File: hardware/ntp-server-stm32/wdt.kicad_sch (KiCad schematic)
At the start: 4 parts, among them U64 TPS3430WDRC

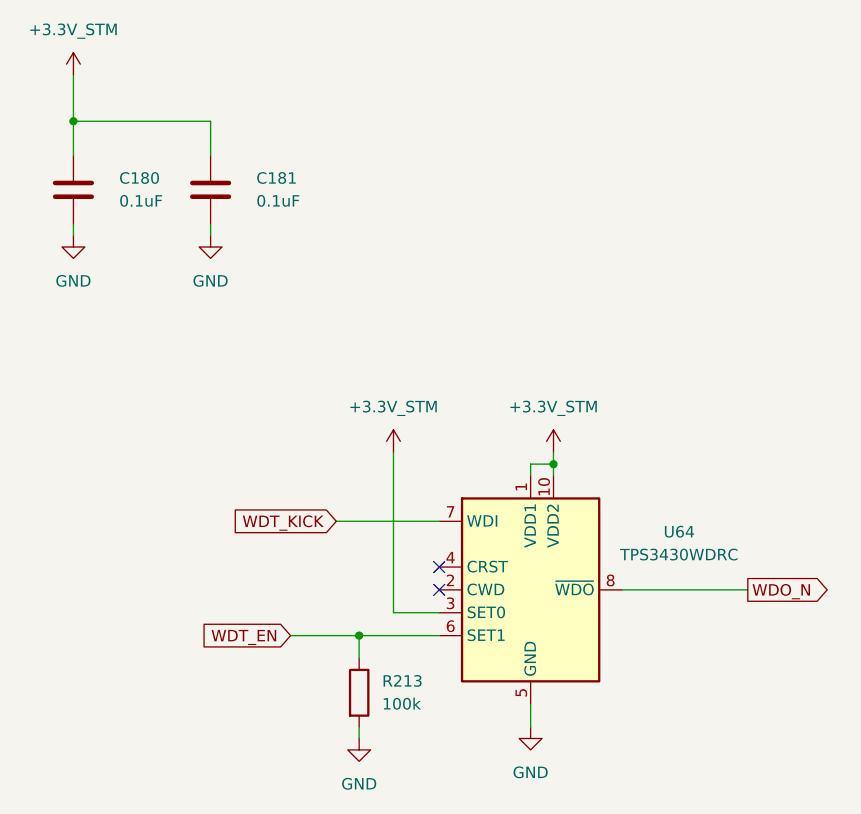
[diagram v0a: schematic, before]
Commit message: Standardize net/rail names: plain 3V3 style, _N active-low, voltage-format PG/alerts
22 net renames applied across all sheets and verified: removed/added net-name
sets match intent exactly and all node connectivity is preserved (kicad-cli
netlist re-parse).

Co-Authored-By: Claude Opus 4.8 (1M context) <noreply@anthropic.com>
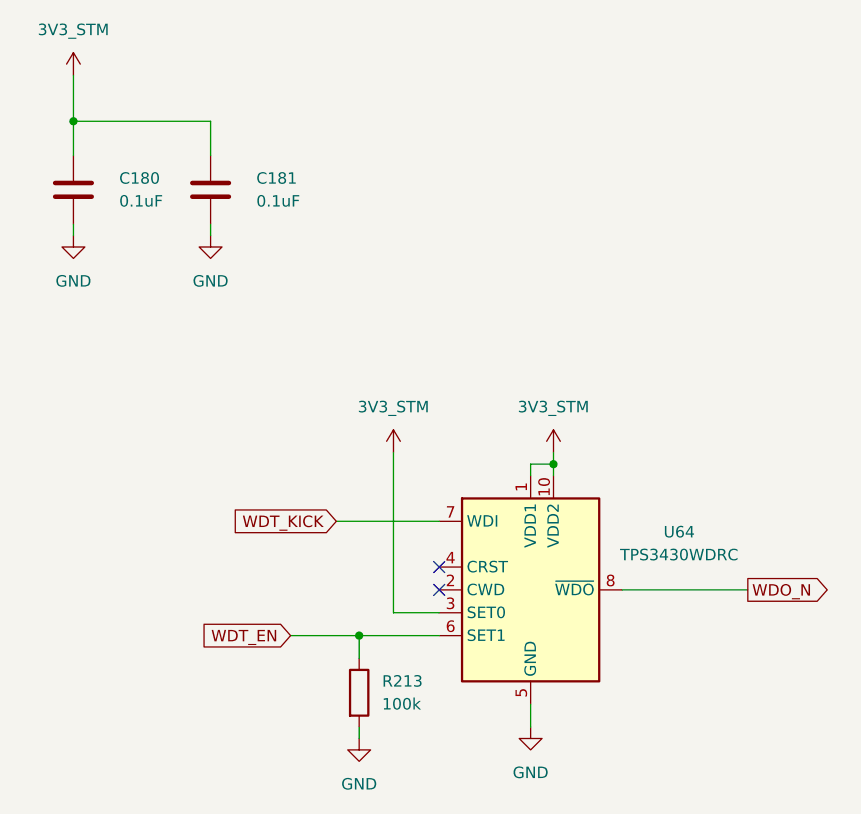
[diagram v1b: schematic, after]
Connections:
- net +3.3V_STM renamed 3V3_STM
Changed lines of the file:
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@@
 			)
 		)
-		(property "Value" "+3.3V_STM"
+		(property "Value" "3V3_STM"
 			(at 148.59 86.36 0)
 			(show_name no)
@@
 			)
 		)
-		(property "Value" "+3.3V_STM"
+		(property "Value" "3V3_STM"
 			(at 166.37 86.36 0)
 			(show_name no)
@@
 			)
 		)
-		(property "Value" "+3.3V_STM"
+		(property "Value" "3V3_STM"
 			(at 113.03 44.45 0)
 			(show_name no)

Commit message: Standardize + complete BOM; write fields back into KiCad symbols
- New sts1000_bom.csv: rebuilt from authoritative Value field (source MPN/footprint/
  description were corrupted by copy-paste). 338 standardized, 78 MPN-from-value,
  50 kept, ~64 flagged (SELECT/REVIEW-HV/SHUNT-REVIEW) each with full spec.
- Resistors -> deterministic Panasonic ERJ-2RKF 0402 1% 1/10W (consolidated 1 part/value).
- Caps -> verified Murata GRM parts where value matches; clean spec + footprint otherwise.
- 1633 symbol field updates (Value/Footprint/Description/MPN/Mfr/Digikey) written to
  .kicad_sch; netlist re-parse confirms connectivity byte-identical.
- Add docs/sts1000_net_naming.md naming reference.

Co-Authored-By: Claude Opus 4.8 (1M context) <noreply@anthropic.com>
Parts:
- C180, C181: footprint 0805 -> C_0402_1005Metric; DIGIKEY_PART_NUMBER 445-5972-1-ND -> 490-6328-2-ND; MANUFACTURER TDK -> Murata; MANUFACTURER_PART_NUMBER C2012X7R1E475K125AB -> GRM155R71C104KA88J
- R213: footprint (none) -> R_0402_1005Metric; MANUFACTURER (none) -> Panasonic; MANUFACTURER_PART_NUMBER (none) -> ERJ-2RKF1003X
- U64: MANUFACTURER_PART_NUMBER (none) -> TPS3430WDRC
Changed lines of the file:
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@@
+			)
+		)
+		(property "MANUFACTURER_PART_NUMBER" "TPS3430WDRC"
+			(at 0 0 0)
+			(hide yes)
+			(show_name no)
+			(do_not_autoplace no)
+			(effects
+				(font
+					(size 1.27 1.27)
+				)
 			)
 		)
@@
 			)
 		)
-		(property "Footprint" ""
+		(property "Footprint" "R_0402_1005Metric"
 			(at 143.002 118.11 90)
 			(hide yes)
@@
 			)
 		)
-		(property "Description" "Resistor"
+		(property "Description" "RES SMD 100k OHM 1% 1/10W 0402"
 			(at 144.78 118.11 0)
+			(hide yes)
+			(show_name no)
+			(do_not_autoplace no)
+			(effects
+				(font
+					(size 1.27 1.27)
+				)
+			)
+		)
+		(property "MANUFACTURER" "Panasonic"
+			(at 0 0 0)
+			(hide yes)
+			(show_name no)
+			(do_not_autoplace no)
+			(effects
+				(font
+					(size 1.27 1.27)
+				)
+			)
+		)
+		(property "MANUFACTURER_PART_NUMBER" "ERJ-2RKF1003X"
+			(at 0 0 0)
 			(hide yes)
 			(show_name no)
@@
 			)
 		)
-		(property "Footprint" "0805"
+		(property "Footprint" "C_0402_1005Metric"
 			(at 129.2352 66.04 0)
 			(hide yes)
@@
 			)
 		)
-		(property "Description" "CAP CER 4.7UF 25V X7R 0805"
+		(property "Description" "CAP CER 0.1uF 16V X7R 0402"
 			(at 128.27 62.23 0)
 			(hide yes)
@@
 			)
 		)
-		(property "DIGIKEY_PART_NUMBER" "445-5972-1-ND"
+		(property "DIGIKEY_PART_NUMBER" "490-6328-2-ND"
 			(at 128.27 62.23 0)
 			(hide yes)
@@
 			)
 		)
-		(property "MANUFACTURER" "TDK"
+		(property "MANUFACTURER" "Murata"
 			(at 128.27 62.23 0)
 			(hide yes)
@@
 			)
 		)
-		(property "MANUFACTURER_PART_NUMBER" "C2012X7R1E475K125AB"
+		(property "MANUFACTURER_PART_NUMBER" "GRM155R71C104KA88J"
 			(at 128.27 62.23 0)
 			(hide yes)
@@
 			)
 		)
-		(property "Footprint" "0805"
+		(property "Footprint" "C_0402_1005Metric"
 			(at 113.9952 66.04 0)
 			(hide yes)
@@
 			)
 		)
-		(property "Description" "CAP CER 4.7UF 25V X7R 0805"
+		(property "Description" "CAP CER 0.1uF 16V X7R 0402"
 			(at 113.03 62.23 0)
 			(hide yes)
@@
 			)
 		)
-		(property "DIGIKEY_PART_NUMBER" "445-5972-1-ND"
+		(property "DIGIKEY_PART_NUMBER" "490-6328-2-ND"
 			(at 113.03 62.23 0)
 			(hide yes)
@@
 			)
 		)
-		(property "MANUFACTURER" "TDK"
+		(property "MANUFACTURER" "Murata"
 			(at 113.03 62.23 0)
 			(hide yes)
@@
 			)
 		)
-		(property "MANUFACTURER_PART_NUMBER" "C2012X7R1E475K125AB"
+		(property "MANUFACTURER_PART_NUMBER" "GRM155R71C104KA88J"
 			(at 113.03 62.23 0)
 			(hide yes)
